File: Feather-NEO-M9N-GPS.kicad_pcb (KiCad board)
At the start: 2 copper layers, 50.8 x 22.9 mm, 61 parts, among them IC1 PRTR5V0U2F,115, J6 USB_B_Micro, U1 NEO-M9N, U2 AP2112K-3.3

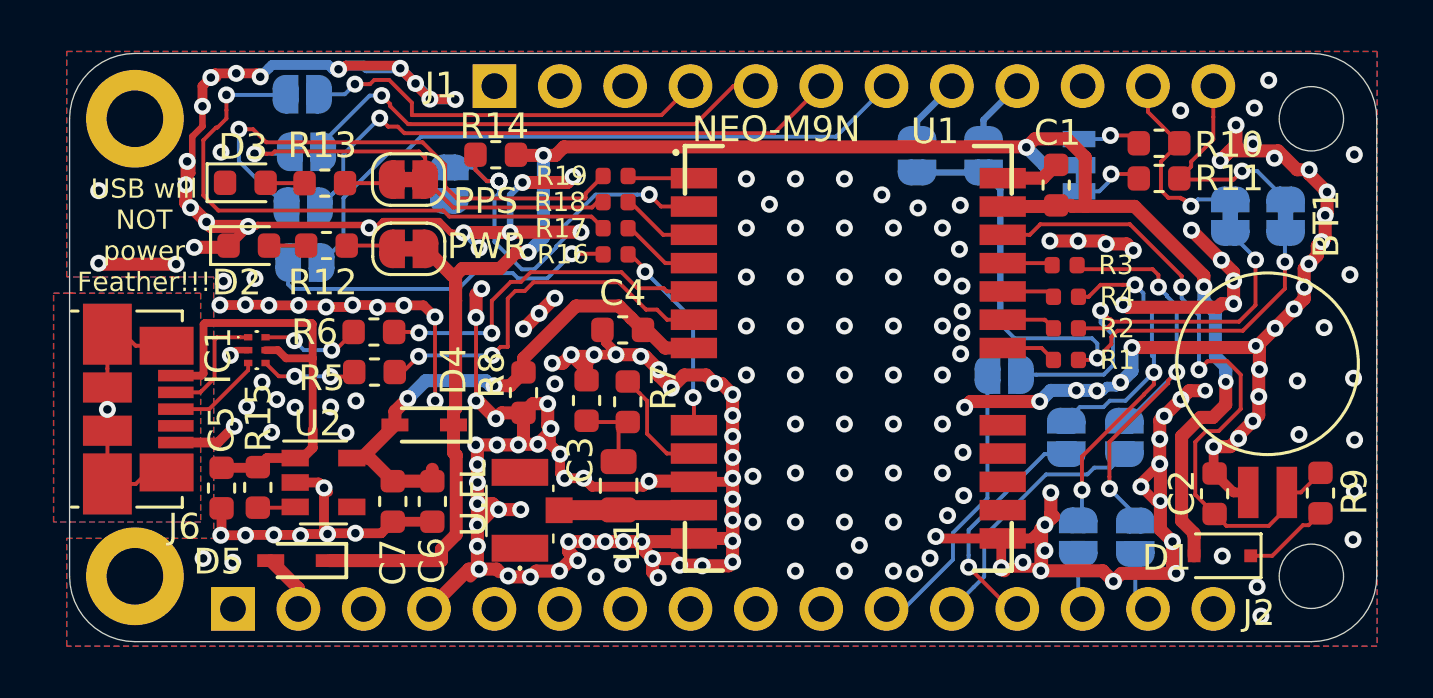
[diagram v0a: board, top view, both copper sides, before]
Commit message: Updated project files to KiCad 9.x
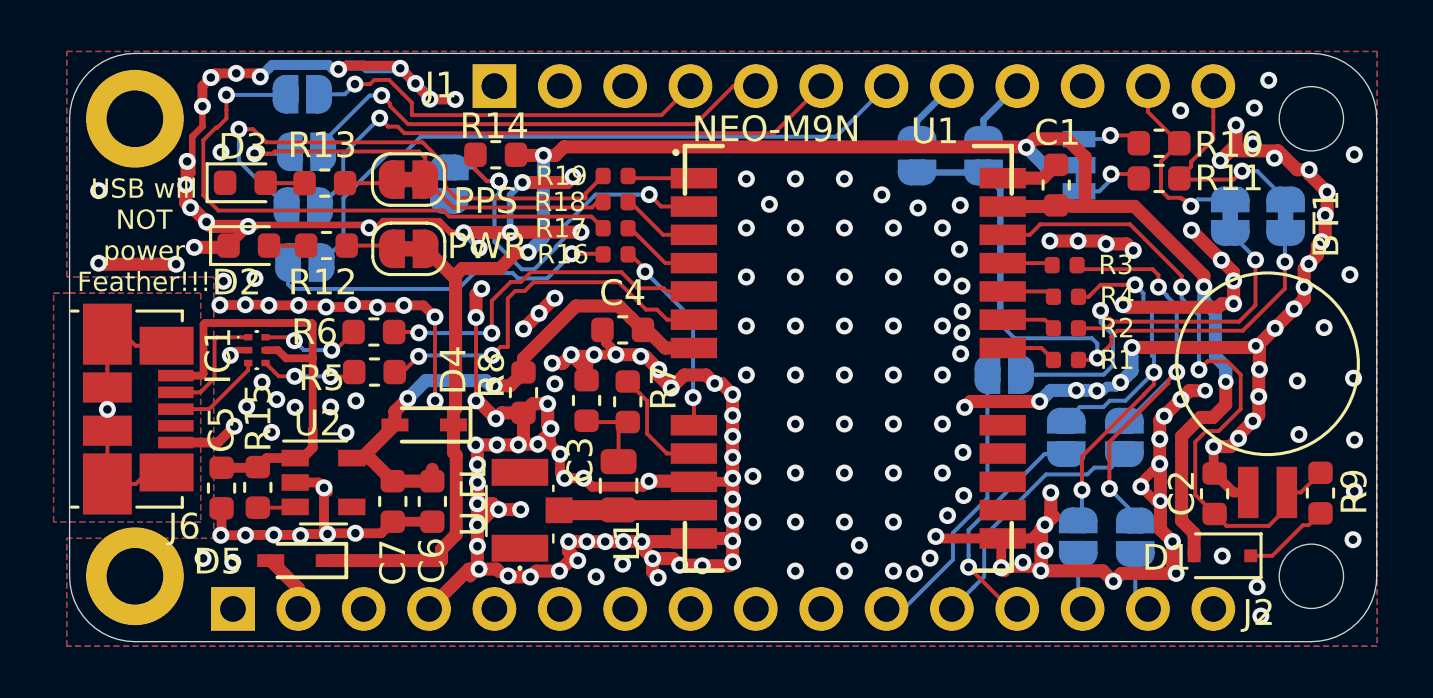
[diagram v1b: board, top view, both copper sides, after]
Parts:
- JP12: value ~SAFE -> ~{SAFE}
- JP16: value ~CS -> ~{CS}
- JP17: value ~CS2 -> ~{CS2}
- JP5: value ~RST GPS -> ~{RST} GPS
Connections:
- net /~RESET_GPS renamed /~{RESET_GPS}
- net /~SAFE renamed /~{SAFE}
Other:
- net class Default removed
- net class RF removed

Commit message: Added missing labels on the bottom layer
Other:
- board text added: "D_SEL"
- board text added: "I2C"
- board text added: "INT"
- board text added: "MISO"
- board text added: "MOSI"
- board text added: "RX"
- board text added: "Rev 2.5 ABW 30/05/25"
- board text added: "SCK"
- board text added: "SCL"
- board text added: "SDA"
- board text added: "TX"
- board text added: "~{CS2}"
- board text added: "~{CS}"
- board text added: "~{RST}"
- board text added: "~{SAFE}"
- board text removed: "10"
- board text removed: "11"
- board text removed: "12"
- board text removed: "13"
- board text removed: "6"
- board text removed: "9"
- board text removed: "Rev2.4 ABW 3/6/20"
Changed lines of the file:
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@@
 		(0 "F.Cu" signal)
 		(2 "B.Cu" signal)
-		(9 "F.Adhes" user)
-		(11 "B.Adhes" user)
+		(9 "F.Adhes" user "F.Adhesive")
+		(11 "B.Adhes" user "B.Adhesive")
 		(13 "F.Paste" user)
 		(15 "B.Paste" user)
-		(5 "F.SilkS" user)
-		(7 "B.SilkS" user)
+		(5 "F.SilkS" user "F.Silkscreen")
+		(7 "B.SilkS" user "B.Silkscreen")
 		(1 "F.Mask" user)
 		(3 "B.Mask" user)
-		(17 "Dwgs.User" user)
-		(19 "Cmts.User" user)
-		(21 "Eco1.User" user)
-		(23 "Eco2.User" user)
+		(17 "Dwgs.User" user "User.Drawings")
+		(19 "Cmts.User" user "User.Comments")
+		(21 "Eco1.User" user "User.Eco1")
+		(23 "Eco2.User" user "User.Eco2")
 		(25 "Edge.Cuts" user)
 		(27 "Margin" user)
-		(31 "F.CrtYd" user)
-		(29 "B.CrtYd" user)
+		(31 "F.CrtYd" user "F.Courtyard")
+		(29 "B.CrtYd" user "B.Courtyard")
 		(35 "F.Fab" user)
 		(33 "B.Fab" user)
@@
 		)
 		(property "Value" "I2C"
-			(at 0.04064 -2.4384 0)
+			(at 1.9558 -2.7178 0)
 			(layer "B.SilkS")
 			(effects
@@
 		)
 		(property "Value" "INT"
-			(at -2.638822 0.01016 0)
+			(at -2.6543 -0.0127 0)
 			(layer "B.SilkS")
 			(effects
@@
 		)
 	)
-	(gr_text "6"
-		(at 165.7604 78.6638 0)
+	(gr_text "I2C"
+		(at 170.434 79.8068 0)
 		(layer "B.SilkS")
 		(effects
@@
 		)
 	)
-	(gr_text "13"
-		(at 140.0175 76.073 0)
+	(gr_text "~{SAFE}"
+		(at 134.3152 80.6196 0)
 		(layer "B.SilkS")
 		(effects
@@
 	)
 	(gr_text "0x42"
-		(at 170.88612 77.73416 0)
+		(at 171.0182 78.0034 0)
 		(layer "B.SilkS")
 		(effects
@@
 		)
 	)
-	(gr_text "12"
-		(at 140.2207 78.2701 0)
+	(gr_text "PPS"
+		(at 134.7978 78.3336 0)
 		(layer "B.SilkS")
 		(effects
@@
 		)
 	)
-	(gr_text "10"
-		(at 140.3477 82.6643 0)
+	(gr_text "Rev 2.5\nABW\n30/05/25"
+		(at 139.60602 90.83294 0)
 		(layer "B.SilkS")
 		(effects
@@
 		)
 	)
-	(gr_text "Rev2.4\nABW\n3/6/20"
-		(at 139.60602 90.83294 0)
+	(gr_text "u-blox GPS\nNEO-M9N\nFeatherwing"
+		(at 154.9908 84.1248 0)
 		(layer "B.SilkS")
 		(effects
@@
 		)
 	)
-	(gr_text "u-blox GPS\nNEO-M9N\nFeatherwing"
-		(at 154.9908 84.1248 0)
+	(gr_text "~{CS} "
+		(at 161.671 81.661 90)
+		(layer "B.SilkS")
+		(effects
+			(font
+				(size 1 1)
+				(thickness 0.15)
+			)
+			(justify mirror)
+		)
+	)
+	(gr_text "MOSI"
+		(at 169.6466 85.9028 90)
+		(layer "B.SilkS")
+		(effects
+			(font
+				(size 1 1)
+				(thickness 0.15)
+			)
+			(justify mirror)
+		)
+	)
+	(gr_text "RX"
+		(at 165.4302 93.2942 0)
+		(layer "B.SilkS")
+		(effects
+			(font
+				(size 1 1)
+				(thickness 0.15)
+			)
+			(justify mirror)
+		)
+	)
+	(gr_text "SDA"
+		(at 176.0474 83.9978 90)
+		(layer "B.SilkS")
+		(effects
+			(font
+				(size 1 1)
+				(thickness 0.15)
+			)
+			(justify mirror)
+		)
+	)
+	(gr_text "SCL"
+		(at 173.6852 83.9978 90)
+		(layer "B.SilkS")
+		(effects
+			(font
+				(size 1 1)
+				(thickness 0.15)
+			)
+			(justify mirror)
+		)
+	)
+	(gr_text "INT"
+		(at 135.001 76.073 0)
+		(layer "B.SilkS")
+		(effects
+			(font
+				(size 1 1)
+				(thickness 0.15)
+			)
+			(justify mirror)
+		)
+	)
+	(gr_text "D_SEL"
+		(at 143.4338 83.439 90)
+		(layer "B.SilkS")
+		(effects
+			(font
+				(size 1 1)
+				(thickness 0.15)
+			)
+			(justify mirror)
+		)
+	)
+	(gr_text "MISO"
+		(at 167.4114 85.852 90)
+		(layer "B.SilkS")
+		(effects
+			(font
+				(size 1 1)
+				(thickness 0.15)
+			)
+			(justify mirror)
+		)
+	)
+	(gr_text "TX"
+		(at 172.3644 93.2942 0)
+		(layer "B.SilkS")
+		(effects
+			(font
+				(size 1 1)
+				(thickness 0.15)
+			)
+			(justify mirror)
+		)
+	)
+	(gr_text "~{RST}"
+		(at 134.8232 82.7024 0)
 		(layer "B.SilkS")
 		(effects
@@
 		)
 	)
-	(gr_text "11"
-		(at 140.1191 80.4037 0)
+	(gr_text "~{CS2}"
+		(at 164.3126 81.7372 90)
 		(layer "B.SilkS")
 		(effects
@@
 		)
 	)
-	(gr_text "9"
-		(at 159.7787 78.6638 0)
+	(gr_text "SCK"
+		(at 161.8742 87.0204 0)
 		(layer "B.SilkS")
 		(effects

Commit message: Removed unnecessary labels
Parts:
- JP5: value ~{RST} GPS -> ~{RST}
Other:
- board text removed: "D_SEL"
- board text removed: "I2C"
- board text removed: "INT"
- board text removed: "MISO"
- board text removed: "MOSI"
- board text removed: "RX"
- board text removed: "SCK"
- board text removed: "SCL"
- board text removed: "SDA"
- board text removed: "TX"
- board text removed: "~{CS}"
- board text removed: "~{RST}"
- board text removed: "~{SAFE}"
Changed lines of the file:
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@@
 		)
 		(property "Value" "I2C"
-			(at 1.9558 -2.7178 0)
+			(at 0.1016 -2.6416 0)
 			(layer "B.SilkS")
 			(effects
@@
 		)
 		(property "Value" "SDA"
-			(at -2.0701 0.5842 180)
+			(at -3.2766 0.0254 270)
 			(layer "B.SilkS")
 			(effects
@@
 		)
 		(property "Value" "SCL"
-			(at -2.1082 -0.49276 180)
+			(at -3.2004 0.04064 270)
 			(layer "B.SilkS")
 			(effects
@@
 		)
 		(property "Value" "TX"
-			(at 0.32512 -2.58826 180)
+			(at -0.00508 -2.20726 180)
 			(layer "B.SilkS")
 			(effects
@@
 		)
 		(property "Value" "RX"
-			(at -0.3937 -2.50698 180)
+			(at 0 -2.27838 180)
 			(layer "B.SilkS")
 			(effects
@@
 		)
 		(property "Value" "INT"
-			(at -2.6543 -0.0127 0)
+			(at -2.7305 -0.0127 0)
 			(layer "B.SilkS")
 			(effects
@@
 		)
 		(property "Value" "PPS"
-			(at -2.972156 0.00508 0)
+			(at -3.0734 0.00508 0)
 			(layer "B.SilkS")
 			(effects
@@
 		)
 		(property "Value" "~{SAFE}"
-			(at -3.28168 0.00508 0)
+			(at -3.4521 0.1651 0)
 			(layer "B.SilkS")
 			(effects
@@
 			)
 		)
-		(property "Value" "~{RST} GPS"
-			(at -4.7625 0.2286 0)
+		(property "Value" "~{RST}"
+			(at -3.0607 0.2286 0)
 			(layer "B.SilkS")
 			(effects
@@
 		)
 		(property "Value" "MISO"
-			(at -0.0762 -2.9337 180)
+			(at -0.0127 -3.0353 180)
 			(layer "B.SilkS")
 			(effects
@@
 		)
 		(property "Value" "MOSI"
-			(at -0.2413 -2.9845 180)
+			(at 0.0127 -3.1369 180)
 			(layer "B.SilkS")
 			(effects
@@
 		)
 		(property "Value" "SPI"
-			(at 0.18288 -2.18694 180)
+			(at 0 -2.4003 180)
 			(layer "B.SilkS")
 			(effects
@@
 		)
 		(property "Value" "~{CS}"
-			(at 2.81686 -1.01346 180)
+			(at 2.82956 -0.25146 270)
 			(layer "B.SilkS")
 			(effects
@@
 		)
 		(property "Value" "SCK"
-			(at -2.8702 0 0)
+			(at -3.0861 0.0381 0)
 			(layer "B.SilkS")
 			(effects
@@
 		)
 		(property "Datasheet" ""
-			(at 0 0 270)
+			(at 0 0 90)
 			(layer "F.Fab")
 			(hide yes)
@@
 		)
 		(property "Description" ""
-			(at 0 0 270)
+			(at 0 0 90)
 			(layer "F.Fab")
 			(hide yes)
@@
 		)
 	)
-	(gr_text "I2C"
-		(at 170.434 79.8068 0)
-		(layer "B.SilkS")
-		(effects
-			(font
-				(size 1 1)
-				(thickness 0.15)
-			)
-			(justify mirror)
-		)
-	)
-	(gr_text "~{SAFE}"
-		(at 134.3152 80.6196 0)
-		(layer "B.SilkS")
-		(effects
-			(font
-				(size 1 1)
-				(thickness 0.15)
-			)
-			(justify mirror)
-		)
-	)
 	(gr_text "0x42"
-		(at 171.0182 78.0034 0)
-		(layer "B.SilkS")
-		(effects
-			(font
-				(size 1 1)
-				(thickness 0.15)
-			)
-			(justify mirror)
-		)
-	)
-	(gr_text "PPS"
-		(at 134.7978 78.3336 0)
+		(at 171.1198 78.0034 0)
 		(layer "B.SilkS")
 		(effects
@@
 		)
 	)
-	(gr_text "~{CS} "
-		(at 161.671 81.661 90)
-		(layer "B.SilkS")
-		(effects
-			(font
-				(size 1 1)
-				(thickness 0.15)
-			)
-			(justify mirror)
-		)
-	)
-	(gr_text "MOSI"
-		(at 169.6466 85.9028 90)
-		(layer "B.SilkS")
-		(effects
-			(font
-				(size 1 1)
-				(thickness 0.15)
-			)
-			(justify mirror)
-		)
-	)
-	(gr_text "RX"
-		(at 165.4302 93.2942 0)
-		(layer "B.SilkS")
-		(effects
-			(font
-				(size 1 1)
-				(thickness 0.15)
-			)
-			(justify mirror)
-		)
-	)
-	(gr_text "SDA"
-		(at 176.0474 83.9978 90)
-		(layer "B.SilkS")
-		(effects
-			(font
-				(size 1 1)
-				(thickness 0.15)
-			)
-			(justify mirror)
-		)
-	)
-	(gr_text "SCL"
-		(at 173.6852 83.9978 90)
-		(layer "B.SilkS")
-		(effects
-			(font
-				(size 1 1)
-				(thickness 0.15)
-			)
-			(justify mirror)
-		)
-	)
-	(gr_text "INT"
-		(at 135.001 76.073 0)
-		(layer "B.SilkS")
-		(effects
-			(font
-				(size 1 1)
-				(thickness 0.15)
-			)
-			(justify mirror)
-		)
-	)
-	(gr_text "D_SEL"
-		(at 143.4338 83.439 90)
-		(layer "B.SilkS")
-		(effects
-			(font
-				(size 1 1)
-				(thickness 0.15)
-			)
-			(justify mirror)
-		)
-	)
-	(gr_text "MISO"
-		(at 167.4114 85.852 90)
-		(layer "B.SilkS")
-		(effects
-			(font
-				(size 1 1)
-				(thickness 0.15)
-			)
-			(justify mirror)
-		)
-	)
-	(gr_text "TX"
-		(at 172.3644 93.2942 0)
-		(layer "B.SilkS")
-		(effects
-			(font
-				(size 1 1)
-				(thickness 0.15)
-			)
-			(justify mirror)
-		)
-	)
-	(gr_text "~{RST}"
-		(at 134.8232 82.7024 0)
-		(layer "B.SilkS")
-		(effects
-			(font
-				(size 1 1)
-				(thickness 0.15)
-			)
-			(justify mirror)
-		)
-	)
 	(gr_text "~{CS2}"
-		(at 164.3126 81.7372 90)
-		(layer "B.SilkS")
-		(effects
-			(font
-				(size 1 1)
-				(thickness 0.15)
-			)
-			(justify mirror)
-		)
-	)
-	(gr_text "SCK"
-		(at 161.8742 87.0204 0)
+		(at 164.338 81.7626 90)
 		(layer "B.SilkS")
 		(effects
